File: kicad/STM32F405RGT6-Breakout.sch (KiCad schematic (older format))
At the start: 56 parts, among them J1 USB_C_Receptacle_USB2.0, J2 Uno Power, J3 SWD/JTAG, J4 Uno Analog, J5 Uno Digital 2, J6 Uno Digital 1, Q1 Si2301CDS, SW1 TS-1187A-B-A-B, SW2 TS-1187A-B-A-B, U1 STM32F405RGT6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

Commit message: Start cutting out 5V plane
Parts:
- J3: footprint Connector_PinSocket_1.27mm:PinSocket_2x05_P1.27mm_Vertical_SMD -> Connector_PinHeader_1.27mm:PinHeader_2x05_P1.27mm_Vertical_SMD
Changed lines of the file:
@@
 F 0 "J3" H 8750 3200 50  0000 C CNN
 F 1 "SWD/JTAG" H 8750 2600 50  0000 C CNN
-F 2 "Connector_PinSocket_1.27mm:PinSocket_2x05_P1.27mm_Vertical_SMD" H 8700 2900 50  0001 C CNN
+F 2 "Connector_PinHeader_1.27mm:PinHeader_2x05_P1.27mm_Vertical_SMD" H 8700 2900 50  0001 C CNN
 F 3 "~" H 8700 2900 50  0001 C CNN
 	1    8700 2900

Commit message: lol, I learned what thermal relief is
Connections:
- net +5V: now also D1.1 (K), FB1.2, Q1.1 (S); no longer F1.2, J1.A4 (VBUS), J1.A9 (VBUS), J1.B4 (VBUS), J1.B9 (VBUS), U3.5 (VBUS)
- new net VBUS: F1.2, J1.A4 (VBUS), J1.A9 (VBUS), J1.B4 (VBUS), J1.B9 (VBUS), U3.5 (VBUS)
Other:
- moved on the sheet: F1
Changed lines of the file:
@@
 USB_CONN_D-
-$Comp
-L power:+5V #PWR038
-U 1 1 61FA3FDE
-P 9800 4125
-F 0 "#PWR038" H 9800 3975 50  0001 C CNN
-F 1 "+5V" H 9815 4298 50  0000 C CNN
-F 2 "" H 9800 4125 50  0001 C CNN
-F 3 "" H 9800 4125 50  0001 C CNN
-	1    9800 4125
-	1    0    0    -1
-$EndComp
 $Comp
 L power:GND #PWR039
@@
 Text Notes 6300 5375 0    50   ~ 0
 The shield is\ngrounded at \nthe host.
-$Comp
-L power:+5V #PWR036
-U 1 1 61F5C05B
-P 8450 3775
-F 0 "#PWR036" H 8450 3625 50  0001 C CNN
-F 1 "+5V" H 8465 3948 50  0000 C CNN
-F 2 "" H 8450 3775 50  0001 C CNN
-F 3 "" H 8450 3775 50  0001 C CNN
-	1    8450 3775
-	1    0    0    -1
-$EndComp
 Wire Wire Line
 	8450 3825 8450 3775
@@
 Wire Wire Line
 	1450 4100 1450 4325
-$Comp
-L power:+5V #PWR0101
-U 1 1 62154291
-P 950 1250
-F 0 "#PWR0101" H 950 1100 50  0001 C CNN
-F 1 "+5V" H 965 1423 50  0000 C CNN
-F 2 "" H 950 1250 50  0001 C CNN
-F 3 "" H 950 1250 50  0001 C CNN
-	1    950  1250
-	1    0    0    -1
-$EndComp
 Wire Wire Line
 	3350 1350 3500 1350
@@
 L Device:Polyfuse_Small F1
 U 1 1 61DD20B4
-P 1275 1350
-F 0 "F1" V 1100 1350 50  0000 C CNN
-F 1 "500mA" V 1175 1350 50  0000 C CNN
-F 2 "Fuse:Fuse_0603_1608Metric" H 1325 1150 50  0001 L CNN
-F 3 "~" H 1275 1350 50  0001 C CNN
-	1    1275 1350
+P 1225 1350
+F 0 "F1" V 1050 1350 50  0000 C CNN
+F 1 "500mA" V 1125 1350 50  0000 C CNN
+F 2 "Fuse:Fuse_0603_1608Metric" H 1275 1150 50  0001 L CNN
+F 3 "~" H 1225 1350 50  0001 C CNN
+	1    1225 1350
 	0    1    1    0
 $EndComp
 Wire Wire Line
-	950  1350 1175 1350
-Wire Wire Line
-	1375 1350 1575 1350
-Wire Wire Line
-	2175 1350 2900 1350
+	950  1350 1125 1350
 $Comp
 L Device:Ferrite_Bead_Small FB2
@@
 	8225 4125 8450 4125
 Connection ~ 8450 4125
+$Comp
+L power:VBUS #PWR?
+U 1 1 622DE4DA
+P 950 1250
+F 0 "#PWR?" H 950 1100 50  0001 C CNN
+F 1 "VBUS" H 965 1423 50  0000 C CNN
+F 2 "" H 950 1250 50  0001 C CNN
+F 3 "" H 950 1250 50  0001 C CNN
+	1    950  1250
+	1    0    0    -1
+$EndComp
+Connection ~ 2475 1350
+Wire Wire Line
+	2475 1250 2475 1350
+$Comp
+L power:+5V #PWR0101
+U 1 1 62154291
+P 2475 1250
+F 0 "#PWR0101" H 2475 1100 50  0001 C CNN
+F 1 "+5V" H 2490 1423 50  0000 C CNN
+F 2 "" H 2475 1250 50  0001 C CNN
+F 3 "" H 2475 1250 50  0001 C CNN
+	1    2475 1250
+	1    0    0    -1
+$EndComp
+Wire Wire Line
+	1325 1350 1575 1350
+Wire Wire Line
+	2175 1350 2475 1350
+Wire Wire Line
+	2475 1350 2900 1350
+$Comp
+L power:VBUS #PWR?
+U 1 1 6231A1B8
+P 8450 3775
+F 0 "#PWR?" H 8450 3625 50  0001 C CNN
+F 1 "VBUS" H 8465 3948 50  0000 C CNN
+F 2 "" H 8450 3775 50  0001 C CNN
+F 3 "" H 8450 3775 50  0001 C CNN
+	1    8450 3775
+	1    0    0    -1
+$EndComp
+$Comp
+L power:VBUS #PWR?
+U 1 1 6231BA00
+P 9800 4125
+F 0 "#PWR?" H 9800 3975 50  0001 C CNN
+F 1 "VBUS" H 9815 4298 50  0000 C CNN
+F 2 "" H 9800 4125 50  0001 C CNN
+F 3 "" H 9800 4125 50  0001 C CNN
+	1    9800 4125
+	1    0    0    -1
+$EndComp
 $EndSCHEMATC

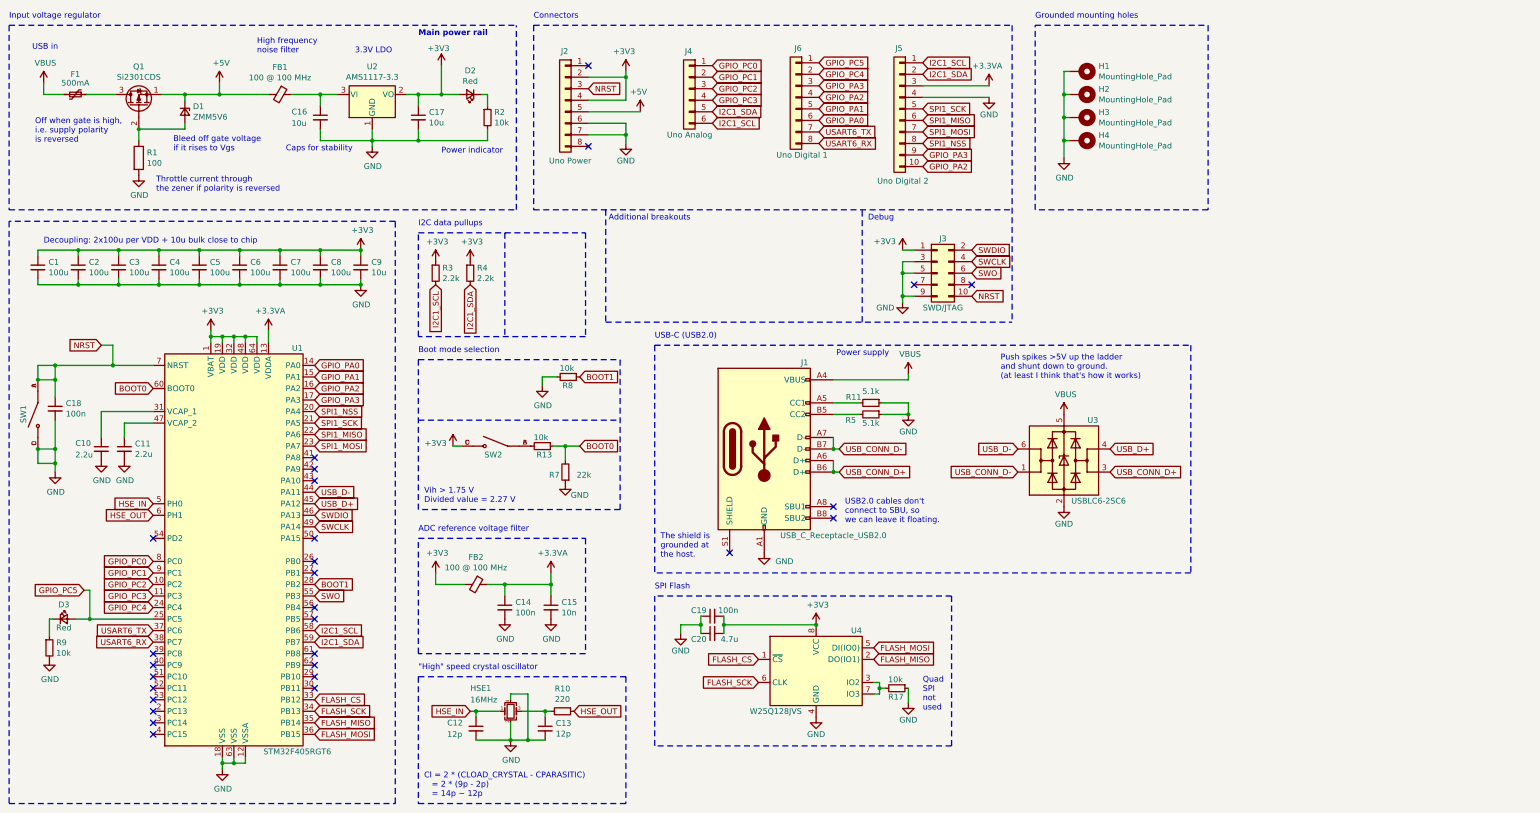
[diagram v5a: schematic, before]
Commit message: SPI flash routed
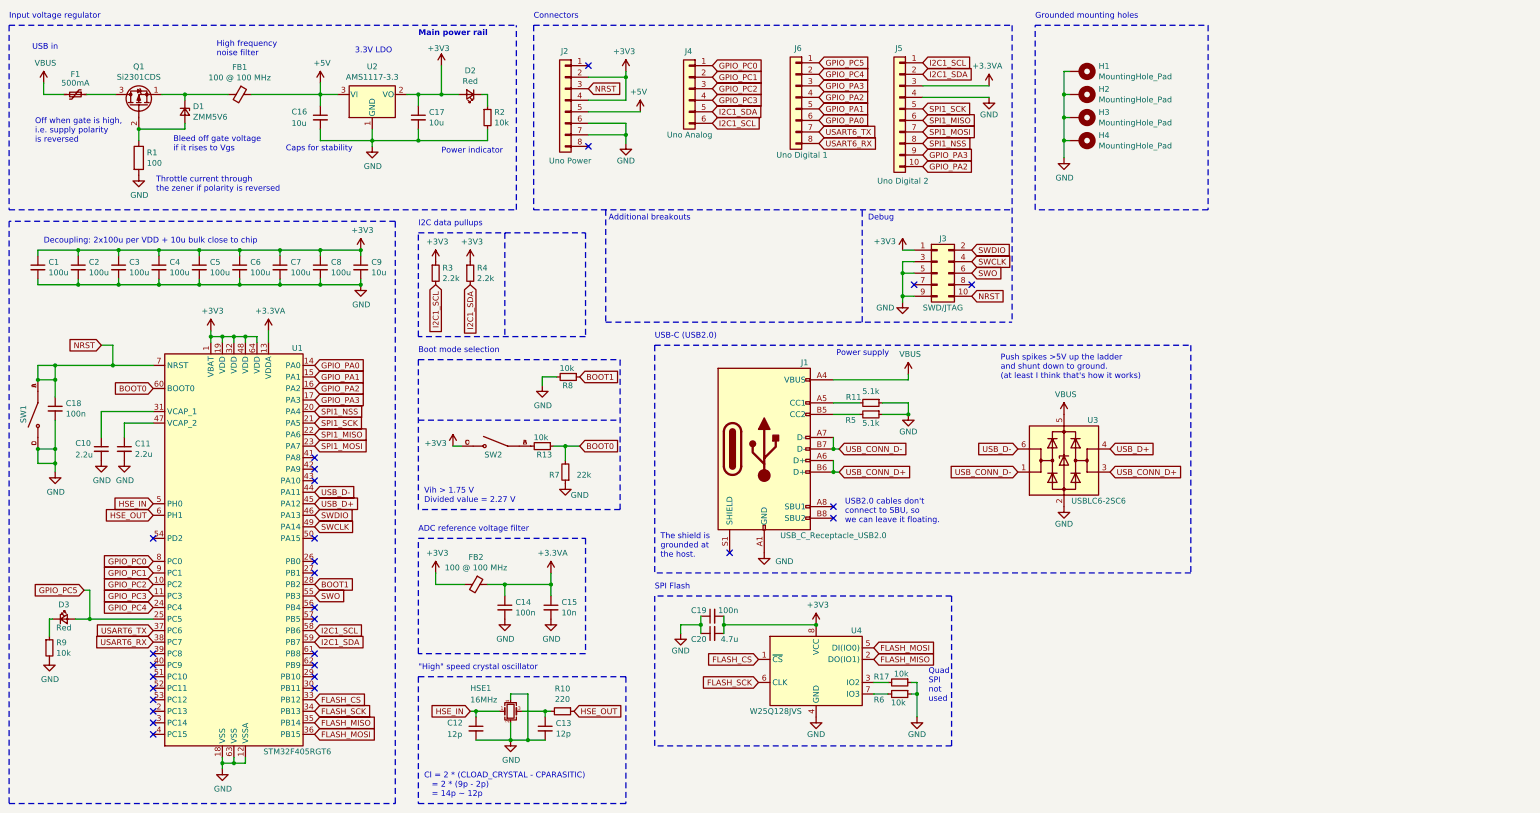
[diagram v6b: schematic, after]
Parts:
- added R6: 10k, Resistor_SMD:R_0402_1005Metric, symbol Device:R_Small
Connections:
- net +5V: now also C16.1, FB1.1, U2.3 (VI); no longer D1.1 (K), FB1.2, Q1.1 (S)
- net GND: now also R6.1
- net at R17.2, U4.3 (IO2): no longer U4.7 (IO3)
- new net: D1.1 (K), FB1.2, Q1.1 (S)
- new net: R6.2, U4.7 (IO3)
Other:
- moved on the sheet: FB1, R17
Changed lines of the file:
@@
 Text Notes 3050 1850 0    50   ~ 0
 Caps for stability\n
-Text Notes 2800 1000 0    50   ~ 0
+Text Notes 2450 1025 0    50   ~ 0
 High frequency \nnoise filter\n
-Connection ~ 2175 1350
 Connection ~ 1775 1650
 Text Notes 3650 1000 0    50   ~ 0
@@
 	0    1    1    0
 $EndComp
-Wire Wire Line
-	3100 1350 3350 1350
 $Comp
 L Device:Ferrite_Bead_Small FB1
 U 1 1 619351E4
-P 3000 1350
-F 0 "FB1" V 2763 1350 50  0000 C CNN
-F 1 "100 @ 100 MHz" V 2854 1350 50  0000 C CNN
-F 2 "Inductor_SMD:L_0805_2012Metric" V 2930 1350 50  0001 C CNN
-F 3 "~" H 3000 1350 50  0001 C CNN
-F 4 "C1015" V 3000 1350 50  0001 C CNN "JLCPCB Part"
-	1    3000 1350
+P 2650 1350
+F 0 "FB1" V 2413 1350 50  0000 C CNN
+F 1 "100 @ 100 MHz" V 2504 1350 50  0000 C CNN
+F 2 "Inductor_SMD:L_0805_2012Metric" V 2580 1350 50  0001 C CNN
+F 3 "~" H 2650 1350 50  0001 C CNN
+F 4 "C1015" V 2650 1350 50  0001 C CNN "JLCPCB Part"
+	1    2650 1350
 	0    1    1    0
 $EndComp
@@
 Text GLabel 8150 6250 2    50   Input ~ 0
 FLASH_MISO
-Text Notes 8575 6700 0    50   ~ 0
+Text Notes 8625 6625 0    50   ~ 0
 Quad\nSPI\nnot\nused
 $Comp
 L power:GND #PWR0104
 U 1 1 619AB58F
-P 8450 6625
-F 0 "#PWR0104" H 8450 6375 50  0001 C CNN
-F 1 "GND" H 8450 6475 50  0000 C CNN
-F 2 "" H 8450 6625 50  0001 C CNN
-F 3 "" H 8450 6625 50  0001 C CNN
-	1    8450 6625
+P 8525 6750
+F 0 "#PWR0104" H 8525 6500 50  0001 C CNN
+F 1 "GND" H 8525 6600 50  0000 C CNN
+F 2 "" H 8525 6750 50  0001 C CNN
+F 3 "" H 8525 6750 50  0001 C CNN
+	1    8525 6750
 	1    0    0    -1
 $EndComp
@@
 L Device:R_Small R17
 U 1 1 6199FF9F
-P 8350 6500
-F 0 "R17" V 8425 6425 50  0000 L CNN
-F 1 "10k" V 8275 6425 50  0000 L CNN
-F 2 "Resistor_SMD:R_0402_1005Metric" H 8350 6500 50  0001 C CNN
-F 3 "~" H 8350 6500 50  0001 C CNN
-	1    8350 6500
+P 8375 6450
+F 0 "R17" V 8325 6225 50  0000 L CNN
+F 1 "10k" V 8300 6400 50  0000 L CNN
+F 2 "Resistor_SMD:R_0402_1005Metric" H 8375 6450 50  0001 C CNN
+F 3 "~" H 8375 6450 50  0001 C CNN
+	1    8375 6450
 	0    1    1    0
 $EndComp
@@
 Text Notes 4250 4900 0    50   ~ 0
 Vih > 1.75 V\nDivided value = 2.27 V
-Wire Wire Line
-	8150 6450 8200 6450
-Wire Wire Line
-	8150 6550 8200 6550
-Wire Wire Line
-	8450 6500 8450 6625
-Wire Wire Line
-	8200 6450 8200 6500
-Wire Wire Line
-	8200 6500 8250 6500
-Connection ~ 8200 6500
-Wire Wire Line
-	8200 6500 8200 6550
 Text GLabel 1900 5500 0    50   Input ~ 0
 GPIO_PC1
@@
 Connection ~ 8450 4125
 $Comp
-L power:VBUS #PWR?
+L power:VBUS #PWR0114
 U 1 1 622DE4DA
 P 950 1250
-F 0 "#PWR?" H 950 1100 50  0001 C CNN
+F 0 "#PWR0114" H 950 1100 50  0001 C CNN
 F 1 "VBUS" H 965 1423 50  0000 C CNN
 F 2 "" H 950 1250 50  0001 C CNN
@@
 	1    0    0    -1
 $EndComp
-Connection ~ 2475 1350
-Wire Wire Line
-	2475 1250 2475 1350
+Wire Wire Line
+	3350 1250 3350 1350
 $Comp
 L power:+5V #PWR0101
 U 1 1 62154291
-P 2475 1250
-F 0 "#PWR0101" H 2475 1100 50  0001 C CNN
-F 1 "+5V" H 2490 1423 50  0000 C CNN
-F 2 "" H 2475 1250 50  0001 C CNN
-F 3 "" H 2475 1250 50  0001 C CNN
-	1    2475 1250
+P 3350 1250
+F 0 "#PWR0101" H 3350 1100 50  0001 C CNN
+F 1 "+5V" H 3365 1423 50  0000 C CNN
+F 2 "" H 3350 1250 50  0001 C CNN
+F 3 "" H 3350 1250 50  0001 C CNN
+	1    3350 1250
 	1    0    0    -1
 $EndComp
 Wire Wire Line
 	1325 1350 1575 1350
-Wire Wire Line
-	2175 1350 2475 1350
-Wire Wire Line
-	2475 1350 2900 1350
-$Comp
-L power:VBUS #PWR?
+$Comp
+L power:VBUS #PWR0115
 U 1 1 6231A1B8
 P 8450 3775
-F 0 "#PWR?" H 8450 3625 50  0001 C CNN
+F 0 "#PWR0115" H 8450 3625 50  0001 C CNN
 F 1 "VBUS" H 8465 3948 50  0000 C CNN
 F 2 "" H 8450 3775 50  0001 C CNN
@@
 $EndComp
 $Comp
-L power:VBUS #PWR?
+L power:VBUS #PWR0116
 U 1 1 6231BA00
 P 9800 4125
-F 0 "#PWR?" H 9800 3975 50  0001 C CNN
+F 0 "#PWR0116" H 9800 3975 50  0001 C CNN
 F 1 "VBUS" H 9815 4298 50  0000 C CNN
 F 2 "" H 9800 4125 50  0001 C CNN
@@
 	1    0    0    -1
 $EndComp
+Wire Wire Line
+	2750 1350 3350 1350
+Wire Wire Line
+	2550 1350 2175 1350
+Connection ~ 2175 1350
+$Comp
+L Device:R_Small R6
+U 1 1 625F6E51
+P 8375 6550
+F 0 "R6" V 8425 6325 50  0000 L CNN
+F 1 "10k" V 8450 6475 50  0000 L CNN
+F 2 "Resistor_SMD:R_0402_1005Metric" H 8375 6550 50  0001 C CNN
+F 3 "~" H 8375 6550 50  0001 C CNN
+	1    8375 6550
+	0    1    1    0
+$EndComp
+Wire Wire Line
+	8150 6450 8275 6450
+Wire Wire Line
+	8150 6550 8275 6550
+Wire Wire Line
+	8475 6450 8525 6450
+Wire Wire Line
+	8525 6450 8525 6550
+Wire Wire Line
+	8475 6550 8525 6550
+Connection ~ 8525 6550
+Wire Wire Line
+	8525 6550 8525 6750
 $EndSCHEMATC
